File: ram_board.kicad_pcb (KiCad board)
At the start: 2 copper layers, 72.1 x 31.6 mm, 18 parts, among them J1 Conn_02x20_Odd_Even, J2 Conn_02x05_Odd_Even, U1 IS61LV5128AL-10TLI, U2 SST39VF040-70-4C-NHE, U3 74LVC04A

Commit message: added switch, switch to 4 layer brd
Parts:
- added SW1: SW_DIP_x04, Button_Switch_SMD:SW_DIP_SPSTx04_Slide_KingTek_DSHP04TS_W7.62mm_P1.27mm, F.Cu at (133.7, 90.8)
- moved R5 5.22 mm to (126.6, 77.9)
- moved D2 5.22 mm to (123.0, 79.8)
- moved D3 5.22 mm to (126.6, 79.8)
- moved R3 5.22 mm to (123.0, 77.9)
- moved R4 5.22 mm to (123.0, 81.7)
- moved U3 5.22 mm to (124.7, 86.6)
- moved C3 5.22 mm to (130.4, 85.6)
- moved R6 5.20 mm to (126.6, 81.6)
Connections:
- J1 pad 20: (no net) -> /SW3
- J1 pad 22: (no net) -> /SW2
- J1 pad 24: (no net) -> /SW1
- J1 pad 26: (no net) -> /SW0
- J1 pad 28: (no net) -> /ROM_WE
- R2 pad 1: Net-(R2-Pad1) -> /ROM_WE
- U2 pad 31: Net-(R2-Pad1) -> /ROM_WE
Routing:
- net +3V3: track 133.2 -> 22.9 mm, vias 9 -> 10
- net /SW0: track 0.00 -> 46.2 mm, vias 0 -> 2
- net /SW1: track 0.00 -> 43.4 mm, vias 0 -> 2
- net /SW2: track 0.00 -> 41.9 mm, vias 0 -> 2
- net /SW3: track 0.00 -> 40.0 mm, vias 0 -> 2
- net /ROM_WE: track 0.00 -> 37.1 mm, vias 0 -> 3
- net /RAM_CE: track 61.2 -> 66.9 mm
- net Net-(R2-Pad1): track 4.02 -> 0.00 mm, vias 1 -> 0
- net GND: track 17.2 -> 20.6 mm, vias 14 -> 25
- net /ROM_CE: track 72.4 -> 75.9 mm
- net /A4: track 59.8 -> 59.1 mm
- net /A14: track 44.1 -> 44.8 mm
- added copper zone on 3V3, net +3V3
- added copper zone on GND, net GND
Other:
- copper layers 2 -> 4

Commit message: fixed labeling
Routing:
- net GND: vias 25 -> 23
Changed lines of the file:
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@@
     (thickness 1.6)
     (drawings 16)
-    (tracks 1026)
+    (tracks 1024)
     (zones 0)
     (modules 19)
@@
   )
   (setup
-    (last_trace_width 0.508)
+    (last_trace_width 0.25)
     (user_trace_width 0.1524)
     (user_trace_width 0.2032)
@@
     (tags "SMD DIP Switch SPST Slide 7.62mm 300mil")
     (attr smd)
-    (fp_text reference SW1 (at 0 -4.4 90) (layer F.SilkS)
+    (fp_text reference SW1 (at 0.0254 -0.0254 180) (layer F.SilkS)
       (effects (font (size 1 1) (thickness 0.15)))
     )
@@
     )
   )
+  (gr_text "DeltaBrd RAM/ROM Extension v1.0\n© 2019 by Hyiger Designs\n\n" (at 136.779 93.218) (layer B.SilkS)
+    (effects (font (size 0.762 0.762) (thickness 0.1524)) (justify mirror))
+  )
   (gr_text ROM (at 126.619 78.4352) (layer F.SilkS)
     (effects (font (size 0.762 0.762) (thickness 0.1524)))
@@
   (gr_line (start 123.444 72.517) (end 117.983 77.978) (layer Edge.Cuts) (width 0.05))
   (gr_line (start 190.119 77.978) (end 184.658 72.517) (layer Edge.Cuts) (width 0.05))
-  (gr_text "DeltaBrd RAM/ROM Extension v1.0\n© 2019 by Hyiger Designs\n\n" (at 136.779 93.218) (layer B.SilkS)
-    (effects (font (size 0.762 0.762) (thickness 0.1524)) (justify mirror))
-  )
   (gr_text RL (at 132.9944 77.8002) (layer B.Cu)
     (effects (font (size 1.016 1.016) (thickness 0.254)) (justify mirror))
@@
   (via (at 182.88 90.8304) (size 0.889) (drill 0.4318) (layers F.Cu B.Cu) (net 1))
   (via (at 177.3174 94.8944) (size 0.889) (drill 0.4318) (layers F.Cu B.Cu) (net 1))
-  (via (at 123.2916 83.4898) (size 0.635) (drill 0.3048) (layers F.Cu B.Cu) (net 1))
+  (via (at 121.2342 80.7466) (size 0.635) (drill 0.3048) (layers F.Cu B.Cu) (net 1))
   (via (at 133.7564 98.425) (size 0.635) (drill 0.3048) (layers F.Cu B.Cu) (net 1))
   (via (at 177.8508 84.5566) (size 0.635) (drill 0.3048) (layers F.Cu B.Cu) (net 1))
@@
   (via (at 179.9336 92.2528) (size 0.635) (drill 0.3048) (layers F.Cu B.Cu) (net 1))
   (via (at 138.7856 82.1182) (size 0.635) (drill 0.3048) (layers F.Cu B.Cu) (net 1))
-  (via (at 144.3228 92.1766) (size 0.508) (drill 0.254) (layers F.Cu B.Cu) (net 1))
-  (via (at 153.3906 92.837) (size 0.508) (drill 0.254) (layers F.Cu B.Cu) (net 1))
   (via (at 158.3436 90.5256) (size 0.508) (drill 0.254) (layers F.Cu B.Cu) (net 1))
   (via (at 155.2702 92.1258) (size 0.508) (drill 0.254) (layers F.Cu B.Cu) (net 1))
@@
   (via (at 120.0404 92.0242) (size 0.889) (drill 0.4318) (layers F.Cu B.Cu) (net 32))
   (segment (start 121.7025 91.9988) (end 120.0658 91.9988) (width 0.508) (layer F.Cu) (net 32) (status 10))
-  (via (at 176.911 75.8444) (size 0.635) (drill 0.3048) (layers F.Cu B.Cu) (net 43))
-  (segment (start 176.276 76.699234) (end 176.372025 76.603209) (width 0.1524) (layer F.Cu) (net 43) (status 30))
-  (segment (start 176.276 77.3545) (end 176.276 76.699234) (width 0.1524) (layer F.Cu) (net 43) (status 30))
-  (segment (start 177.913 74.8424) (end 176.911 75.8444) (width 0.2032) (layer B.Cu) (net 43) (status 10))
-  (segment (start 177.913 74.803) (end 177.913 74.8424) (width 0.2032) (layer B.Cu) (net 43) (status 30))
-  (segment (start 176.276 76.4794) (end 176.911 75.8444) (width 0.2032) (layer F.Cu) (net 43) (status 10))
-  (segment (start 176.276 77.3545) (end 176.276 76.4794) (width 0.2032) (layer F.Cu) (net 43) (status 30))
   (segment (start 187.214799 91.490799) (end 180.306 84.582) (width 0.1524) (layer F.Cu) (net 33) (status 20))
   (segment (start 187.214799 99.076799) (end 187.214799 91.490799) (width 0.1524) (layer F.Cu) (net 33))
@@
   (segment (start 126.3296 80.0608) (end 126.66739 80.39859) (width 0.1524) (layer F.Cu) (net 42))
   (segment (start 125.7046 80.0608) (end 126.3296 80.0608) (width 0.1524) (layer F.Cu) (net 42) (status 10))
+  (via (at 176.911 75.8444) (size 0.635) (drill 0.3048) (layers F.Cu B.Cu) (net 43))
+  (segment (start 176.276 76.699234) (end 176.372025 76.603209) (width 0.1524) (layer F.Cu) (net 43) (status 30))
+  (segment (start 176.276 77.3545) (end 176.276 76.699234) (width 0.1524) (layer F.Cu) (net 43) (status 30))
+  (segment (start 177.913 74.8424) (end 176.911 75.8444) (width 0.2032) (layer B.Cu) (net 43) (status 10))
+  (segment (start 177.913 74.803) (end 177.913 74.8424) (width 0.2032) (layer B.Cu) (net 43) (status 30))
+  (segment (start 176.276 76.4794) (end 176.911 75.8444) (width 0.2032) (layer F.Cu) (net 43) (status 10))
+  (segment (start 176.276 77.3545) (end 176.276 76.4794) (width 0.2032) (layer F.Cu) (net 43) (status 30))
   (segment (start 171.974799 99.076799) (end 171.974799 96.460599) (width 0.1524) (layer F.Cu) (net 43))
   (segment (start 173.101 100.203) (end 171.974799 99.076799) (width 0.1524) (layer F.Cu) (net 43) (status 10))

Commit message: redesign
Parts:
- removed R4, R5, R6: 360R, Resistor_SMD:R_0603_1608Metric_Pad1.05x0.95mm_HandSolder
- removed U3: 74LVC04A, Package_SO:TSSOP-14_4.4x5mm_P0.65mm
- added R1: 360R, Resistor_SMD:R_0603_1608Metric_Pad1.05x0.95mm_HandSolder, B.Cu at (142.1, 80.0)
- added RN1: 1K, Resistor_SMD:R_Array_Convex_4x1206, B.Cu at (129.9, 83.2)
- added U4: 74LVC2G04, Package_SO:TSOP-6_1.65x3.05mm_P0.95mm, F.Cu at (142.1, 85.1)
- added U5: 74LVC2G04, Package_SO:TSOP-6_1.65x3.05mm_P0.95mm, F.Cu at (161.8, 85.0)
- J1: value Conn_02x20_Odd_Even -> Bus
- J2: value Conn_02x05_Odd_Even -> PWR
- R2: value 10K -> 1K
- SW1: value SW_DIP_x04 -> Config; footprint Button_Switch_SMD:SW_DIP_SPSTx04_Slide_KingTek_DSHP04TS_W7.62mm_P1.27mm -> Button_Switch_SMD:SW_DIP_SPSTx06_Slide_KingTek_DSHP06TS_W7.62mm_P1.27mm
- moved R3 38.7 mm to (161.7, 80.4), turned to 0 degrees
- moved D3 35.3 mm to (161.8, 82.2)
- moved D2 19.2 mm to (142.1, 81.9)
- moved C3 11.2 mm to (140.1, 91.2)
- moved SW1 8.41 mm to (129.9, 83.3)
- moved C4 1.32 mm to (124.3, 92.7), turned to 180 degrees
- moved C5 1.15 mm to (124.3, 95.0), turned to 180 degrees
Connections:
- D2 pad 3: Net-(D2-Pad3) -> Net-(D2-Pad1)
- D3 pad 3: Net-(D3-Pad3) -> Net-(D3-Pad1)
- J1 pad 1: /A0 -> GND
- J1 pad 10: /A9 -> /A1
- J1 pad 11: /A10 -> /A2
- J1 pad 12: /A11 -> /A3
- J1 pad 13: /A12 -> /A4
- J1 pad 14: /A13 -> /A5
- J1 pad 15: /A14 -> /A8
- J1 pad 16: /A15 -> /A7
- J1 pad 17: /A16 -> /A10
- J1 pad 18: /A17 -> /A9
- J1 pad 19: /A18 -> /A12
- J1 pad 2: /A1 -> /SW1_3
- J1 pad 20: /SW3 -> /A11
- J1 pad 21: /RAM_CE -> /A14
- J1 pad 22: /SW2 -> /A13
- J1 pad 23: /RAM_OE -> /A16
- J1 pad 24: /SW1 -> /A15
- J1 pad 25: /RAM_WE -> /A18
- J1 pad 26: /SW0 -> /A17
- J1 pad 27: /D0 -> /RAM_OE
- J1 pad 28: /ROM_WE -> /RAM_CE
- J1 pad 29: /D1 -> /D0
- J1 pad 3: /A2 -> (no net)
- J1 pad 30: /D2 -> /RAM_WE
- J1 pad 31: /D3 -> /D2
- J1 pad 32: GND -> /D1
- J1 pad 33: GND -> /D4
- J1 pad 34: /D4 -> /D3
- J1 pad 39: GND -> /ROM_WE
- J1 pad 4: /A3 -> /SW1_2
- J1 pad 5: /A4 -> (no net)
- J1 pad 6: /A5 -> /SW1_1
- J1 pad 7: /A6 -> (no net)
- J1 pad 8: /A7 -> /SW1_0
- J1 pad 9: /A8 -> /A0
- J2 pad 1: (no net) -> GND
- J2 pad 10: GND -> (no net)
- J2 pad 2: (no net) -> GND
- J2 pad 3: +3V3 -> GND
- J2 pad 4: +3V3 -> GND
- J2 pad 7: GND -> +3V3
- J2 pad 8: GND -> +3V3
- J2 pad 9: GND -> (no net)
- R3 pad 1: Net-(D2-Pad1) -> Net-(D3-Pad1)
- SW1 pad 5: /SW3 -> GND
- SW1 pad 6: /SW2 -> GND
- SW1 pad 7: /SW1 -> (no net)
- SW1 pad 8: /SW0 -> (no net)
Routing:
- net /ROM_CE: track 75.9 -> 0.00 mm, vias 2 -> 0
- net /A8: track 71.4 -> 0.00 mm, vias 4 -> 0
- net /A9: track 70.7 -> 0.00 mm, vias 4 -> 0
- net /RAM_CE: track 66.9 -> 0.00 mm, vias 4 -> 0
- net /A1: track 65.9 -> 0.00 mm, vias 4 -> 0
- net /A3: track 65.2 -> 0.00 mm, vias 4 -> 0
- net /A7: track 64.5 -> 0.00 mm, vias 4 -> 0
- net /A0: track 64.0 -> 0.00 mm, vias 4 -> 0
- net /A2: track 61.3 -> 0.00 mm, vias 4 -> 0
- net /A5: track 61.2 -> 0.00 mm, vias 4 -> 0
- net /A6: track 60.6 -> 0.00 mm, vias 4 -> 0
- net /A4: track 59.1 -> 0.00 mm, vias 4 -> 0
- net /D2: track 54.0 -> 0.00 mm, vias 2 -> 0
- net /D0: track 53.6 -> 0.00 mm, vias 2 -> 0
- net /D1: track 52.2 -> 0.00 mm, vias 2 -> 0
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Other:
- board text added: "1"
- board text added: "16"
- board text added: "2"
- board text added: "32"
- board text added: "4"
- board text added: "8"
- board text added: "Config"
- board text added: "MAX V RAM/ROM Extension v1.0 © 2019 by Hyiger Designs Made for: DeltaBrd http://ilchev.net/deltabrd"
- board text added: "RAM Ena"
- board text added: "ROM Ena"
- board text removed: "DeltaBrd RAM/ROM Extension v1.0 © 2019 by Hyiger Designs"
- board text removed: "ENA"
- board text removed: "RAM"
- board text removed: "ROM"

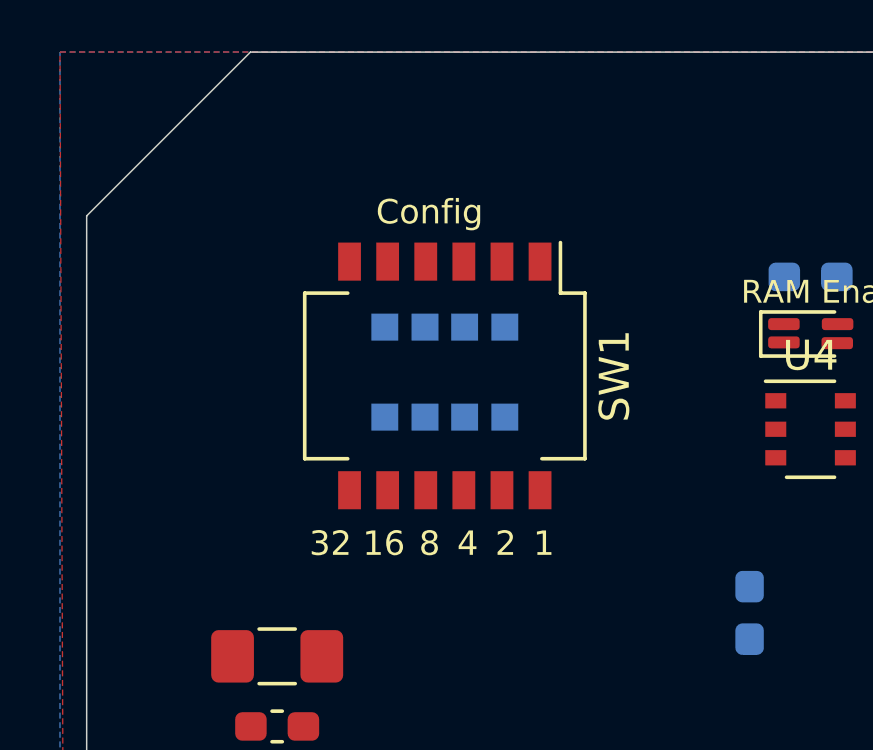
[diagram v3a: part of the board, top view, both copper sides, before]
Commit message: tri-state led driver
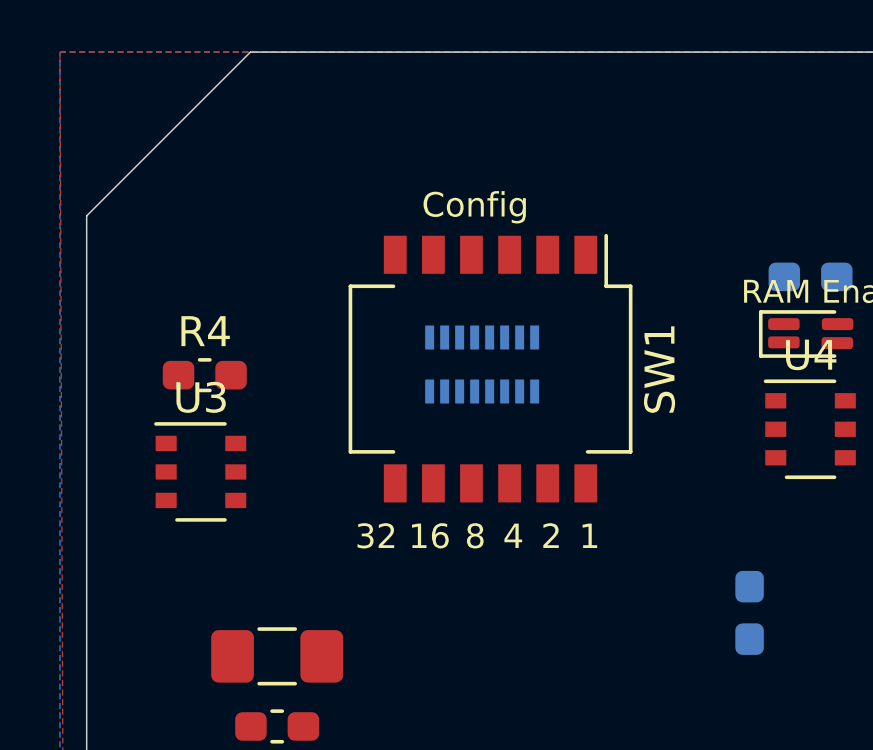
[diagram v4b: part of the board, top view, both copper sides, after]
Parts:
- added R4: 360R, Resistor_SMD:R_0603_1608Metric_Pad1.05x0.95mm_HandSolder, F.Cu at (121.9, 83.3)
- added U3: 74LVC2G04, Package_SO:TSOP-6_1.65x3.05mm_P0.95mm, F.Cu at (121.8, 86.5)
- RN1: value 1K -> R_Network06; footprint Resistor_SMD:R_Array_Convex_4x1206 -> Resistor_SMD:R_Array_Convex_8x0602
- moved SW1 1.54 mm to (131.4, 83.1)
- moved RN1 1.27 mm to (131.2, 82.9)
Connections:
- J1 pad 3: (no net) -> /SW1_5
- J1 pad 5: (no net) -> /SW1_4
- J1 pad 7: (no net) -> /LED1
- RN1 pad 1: /SW1_0 -> +3V3
- RN1 pad 2: /SW1_1 -> /SW1_0
- RN1 pad 3: /SW1_2 -> /SW1_1
- RN1 pad 4: /SW1_3 -> /SW1_2
- RN1 pad 5: +3V3 -> /SW1_3
- RN1 pad 6: +3V3 -> /SW1_4
- RN1 pad 7: +3V3 -> /SW1_5
- RN1 pad 8: +3V3 -> (no net)
- SW1 pad 7: (no net) -> /SW1_5
- SW1 pad 8: (no net) -> /SW1_4

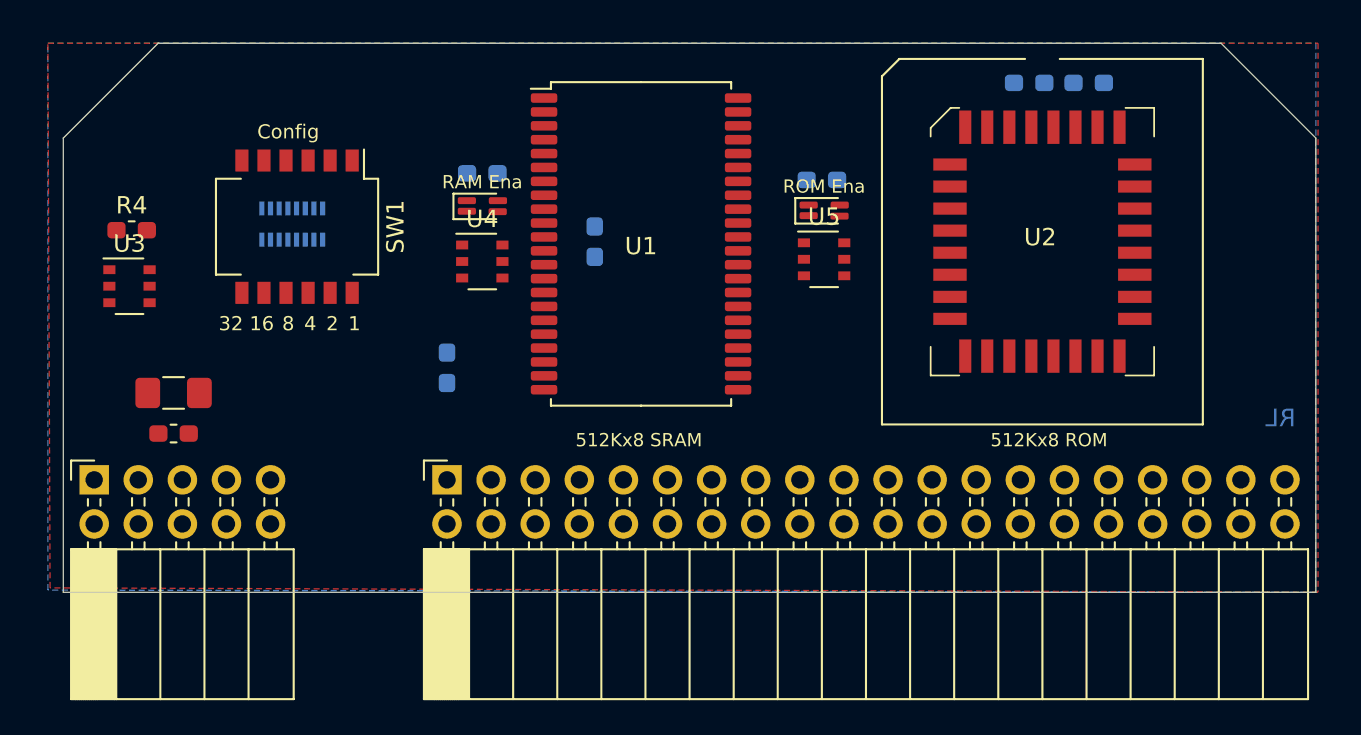
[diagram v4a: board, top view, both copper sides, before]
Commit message: switched to discrete resistors,
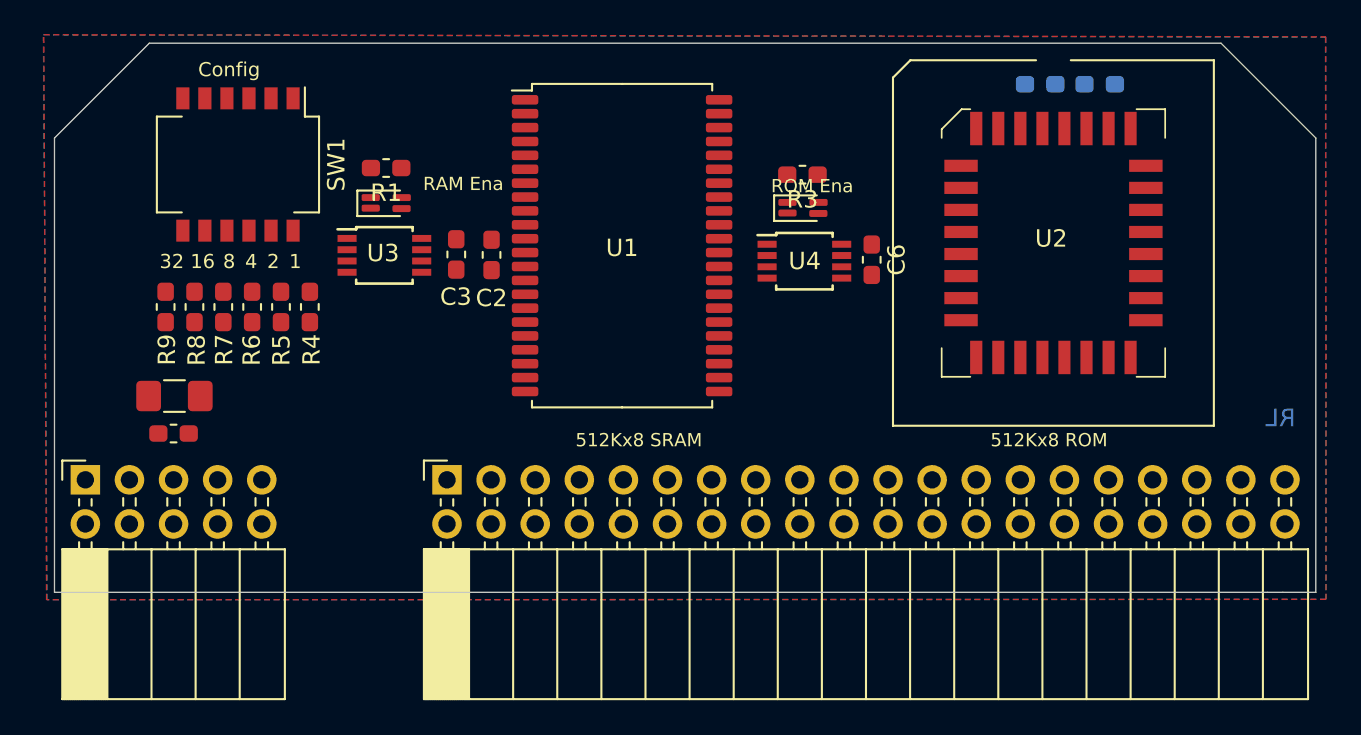
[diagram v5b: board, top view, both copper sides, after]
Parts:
- removed RN1: R_Network06, Resistor_SMD:R_Array_Convex_8x0602
- removed U5: 74LVC2G04, Package_SO:TSOP-6_1.65x3.05mm_P0.95mm
- added C6: 100nF, Capacitor_SMD:C_0603_1608Metric_Pad1.05x0.95mm_HandSolder, F.Cu at (164.5, 85.0)
- added R5: 10K, Resistor_SMD:R_0603_1608Metric_Pad1.05x0.95mm_HandSolder, F.Cu at (130.5, 87.7)
- added R6: 10K, Resistor_SMD:R_0603_1608Metric_Pad1.05x0.95mm_HandSolder, F.Cu at (128.9, 87.7)
- added R7: 10K, Resistor_SMD:R_0603_1608Metric_Pad1.05x0.95mm_HandSolder, F.Cu at (127.2, 87.7)
- added R8: 10K, Resistor_SMD:R_0603_1608Metric_Pad1.05x0.95mm_HandSolder, F.Cu at (125.5, 87.7)
- added R9: 10K, Resistor_SMD:R_0603_1608Metric_Pad1.05x0.95mm_HandSolder, F.Cu at (123.9, 87.7)
- C2, C3, R1, R3: moved to F.Cu
- R2: value 1K -> 10K
- R4: value 360R -> 10K
- U3, U4: value 74LVC2G04 -> 74LVC2G240; footprint Package_SO:TSOP-6_1.65x3.05mm_P0.95mm -> Package_SO:TSSOP-8_3x3mm_P0.65mm
- moved U4 18.6 mm to (160.7, 85.1)
- moved U3 14.8 mm to (136.5, 84.7)
- moved R4 11.2 mm to (132.2, 87.7), turned to 270 degrees
- moved C3 6.55 mm to (140.6, 84.7)
- moved C2 5.99 mm to (142.6, 84.7)
- moved R1 5.55 mm to (136.6, 79.7)
- moved D2 5.54 mm to (136.6, 81.7)
- moved SW1 4.94 mm to (128.0, 79.5)
- moved D3 1.23 mm to (160.6, 82.0)
- moved R3 1.16 mm to (160.6, 80.1), turned to 180 degrees
- moved U1 1.10 mm to (150.2, 84.2)
- moved C1 0.64 mm to (174.2, 74.9)
- moved R2 0.64 mm to (177.7, 74.9)
- moved U2 0.64 mm to (175.0, 84.0)
- moved J2 0.51 mm to (119.3, 97.7)
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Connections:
- J1 pad 7: /LED1 -> (no net)
- R4 pad 1: (no net) -> /SW1_0
- R4 pad 2: Net-(R4-Pad2) -> +3V3
- U3 pad 1: /LED1 -> /~ENA
- U3 pad 2: GND -> /RAM_CE
- U3 pad 3: (no net) -> Net-(D2-Pad4)
- U3 pad 4: (no net) -> GND
- U3 pad 5: +3V3 -> Net-(D2-Pad2)
- U3 pad 6: Net-(R4-Pad2) -> Net-(D2-Pad2)
- U4 pad 1: /RAM_CE -> /~ENA
- U4 pad 2: GND -> /ROM_CE
- U4 pad 3: Net-(D2-Pad2) -> Net-(D3-Pad4)
- U4 pad 4: Net-(D2-Pad4) -> GND
- U4 pad 5: +3V3 -> Net-(D3-Pad2)
- U4 pad 6: Net-(D2-Pad2) -> Net-(D3-Pad2)
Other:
- board size 72.1 x 31.6 mm -> 72.6 x 31.6 mm

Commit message: simplified pins, finished routing
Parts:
- removed R4: 10K, Resistor_SMD:R_0603_1608Metric_Pad1.05x0.95mm_HandSolder
- added C7: 100nF, Capacitor_SMD:C_0603_1608Metric_Pad1.05x0.95mm_HandSolder, F.Cu at (156.9, 84.6)
- added U5: 74LVC2G32, Package_SO:TSSOP-8_3x3mm_P0.65mm, F.Cu at (160.9, 91.5)
- R2: moved to F.Cu
- moved R2 48.3 mm to (131.1, 87.7), turned to 270 degrees
- moved D2 4.22 mm to (140.7, 80.8)
- moved R1 4.18 mm to (140.6, 78.8)
- moved R3 3.65 mm to (163.8, 78.5)
- moved D3 3.59 mm to (163.8, 80.5)
- moved R5 1.09 mm to (129.4, 87.7)
- moved R6 1.09 mm to (127.8, 87.7)
- moved R7 1.09 mm to (126.1, 87.7)
- moved SW1 1.09 mm to (126.9, 79.5)
- moved R8 1.09 mm to (124.4, 87.7)
- moved R9 1.09 mm to (122.8, 87.7)
- moved C2 1.04 mm to (141.6, 84.6)
- moved U1 0.89 mm to (149.3, 84.2)
- moved C3 0.89 mm to (139.7, 84.6)
- moved U3 0.76 mm to (135.7, 84.8)
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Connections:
- J1 pad 11: /A2 -> /A4
- J1 pad 13: /A4 -> /A6
- J1 pad 2: /SW1_3 -> /SW1_5
- J1 pad 27: /RAM_OE -> (no net)
- J1 pad 28: /RAM_CE -> /~ENA
- J1 pad 29: /D0 -> /~ROM
- J1 pad 3: /SW1_5 -> /SW1_3
- J1 pad 30: /RAM_WE -> /~RAM
- J1 pad 31: /D2 -> /~RD
- J1 pad 32: /D1 -> /~WR
- J1 pad 33: /D4 -> /D0
- J1 pad 34: /D3 -> /D1
- J1 pad 35: /D6 -> /D2
- J1 pad 36: /D5 -> /D3
- J1 pad 37: /ROM_CE -> /D4
- J1 pad 38: /D7 -> /D5
- J1 pad 39: /ROM_WE -> /D6
- J1 pad 4: /SW1_2 -> /SW1_4
- J1 pad 40: /ROM_OE -> /D7
- J1 pad 5: /SW1_4 -> /SW1_1
- J1 pad 6: /SW1_1 -> /SW1_2
- J1 pad 7: (no net) -> /A0
- J1 pad 9: /A0 -> /A2
- R2 pad 1: /ROM_WE -> /SW1_0
- U1 pad 15: /RAM_WE -> /~WR
- U1 pad 37: /RAM_OE -> /~RD
- U1 pad 8: /RAM_CE -> Net-(U1-Pad8)
- U2 pad 22: /ROM_CE -> Net-(U2-Pad22)
- U2 pad 24: /ROM_OE -> /~RD
- U2 pad 31: /ROM_WE -> /~WR
- U3 pad 2: /RAM_CE -> (no net)
- U4 pad 2: /ROM_CE -> (no net)
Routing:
- net /~ENA: track 0.00 -> 98.3 mm, vias 0 -> 8
- net /D6: track 0.00 -> 71.5 mm, vias 0 -> 4
- net /A7: track 0.00 -> 71.2 mm, vias 0 -> 5
- net /D7: track 0.00 -> 67.5 mm, vias 0 -> 4
- net /~WR: track 0.00 -> 65.5 mm, vias 0 -> 4
- net /D5: track 0.00 -> 62.1 mm, vias 0 -> 4
- net /D4: track 0.00 -> 62.0 mm, vias 0 -> 4
- net /D1: track 0.00 -> 58.4 mm, vias 0 -> 6
- net /A9: track 0.00 -> 57.5 mm, vias 0 -> 4
- net /D3: track 0.00 -> 56.4 mm, vias 0 -> 4
- net /D2: track 0.00 -> 55.8 mm, vias 0 -> 5
- net /A0: track 0.00 -> 55.8 mm, vias 0 -> 2
- net /A8: track 0.00 -> 55.3 mm, vias 0 -> 4
- net /A1: track 0.00 -> 55.2 mm, vias 0 -> 4
- net /A2: track 0.00 -> 55.0 mm, vias 0 -> 4
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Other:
- rule via_min_drill: 0.254 -> 0.2032
- rule via_min_size: 0.508 -> 0.4064
